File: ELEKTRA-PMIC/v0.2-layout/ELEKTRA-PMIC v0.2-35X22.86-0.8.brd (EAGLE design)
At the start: 35 x 22.9 mm, 96 parts, among them U1 BQ24195L, U4 MAX1704X

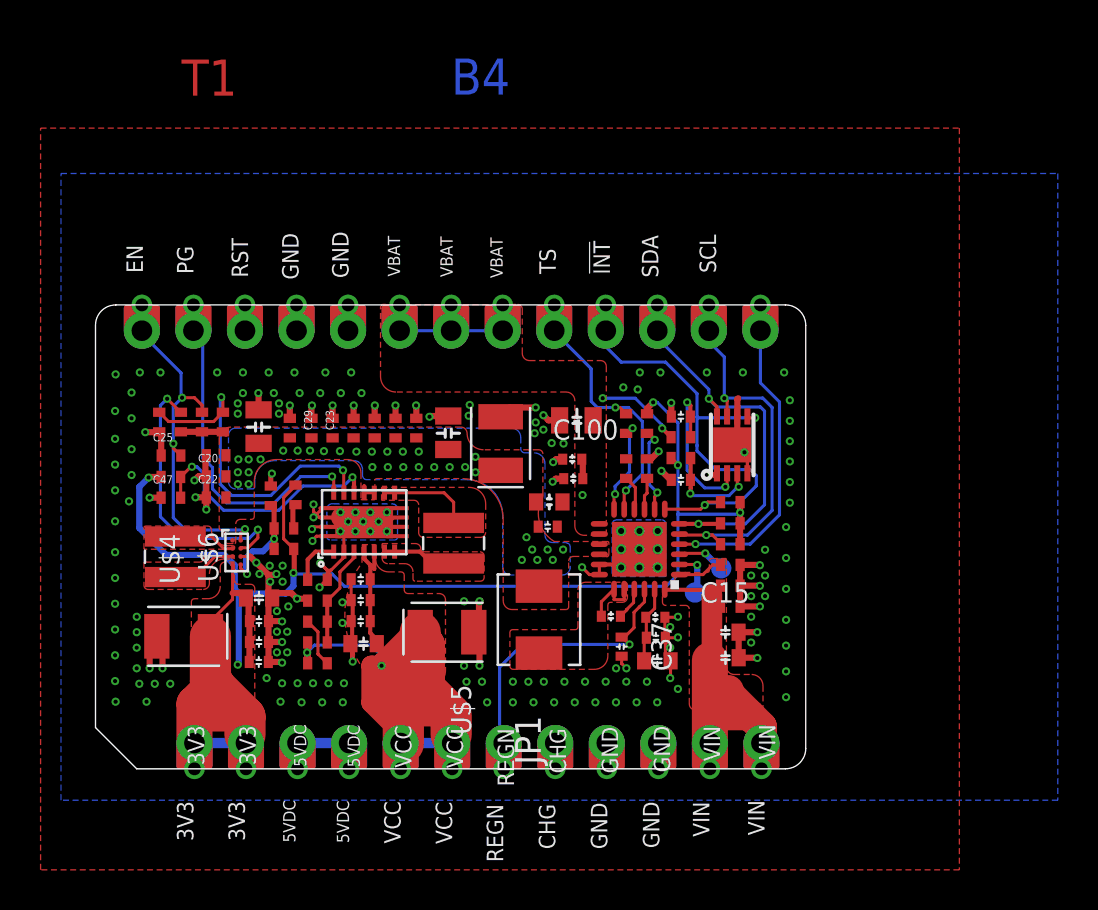
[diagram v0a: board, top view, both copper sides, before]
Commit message: update layout
complete the layout for power module
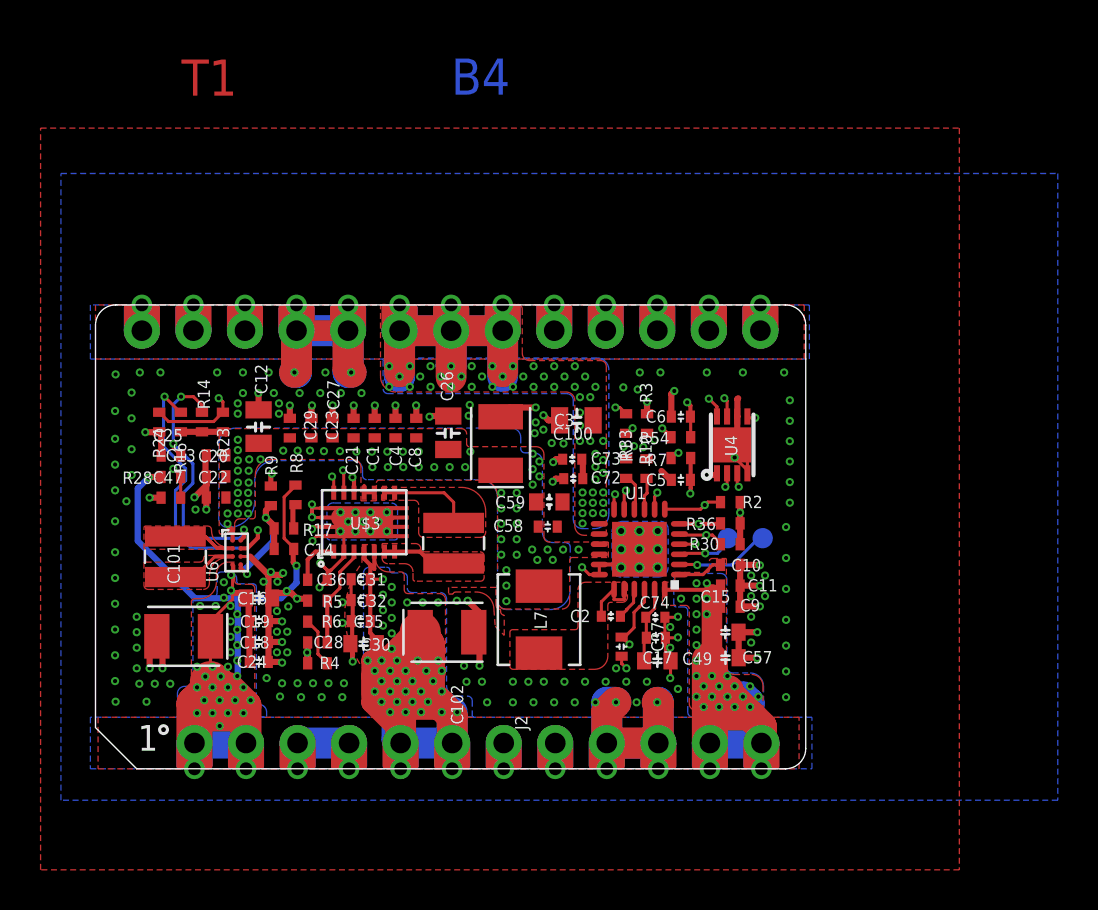
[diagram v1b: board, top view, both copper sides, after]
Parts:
- removed TP20, TP21, TP22: TP0.4MM, particle SZ:TP0.4MM
- C101: value CAP-ECASE_B -> 220uF.6V
- C102: value CAP-ECASE_B -> 220uF,6V
- TP10, TP11, TP3, TP4, TP5, TP6, TP7, TP8, TP9: value TP -> TP0.4MM; device particle SZ:TP0.7MM -> particle SZ:TP0.4MM
- moved TP1 4.28 mm to (32.9, 11.4)
- moved TP2 1.52 mm to (31.2, 11.4)
- moved TP17 0.60 mm to (12.8, 11.7)
- renumbered JP1 to J2, U$1 to J1, U$4 to C101, U$5 to C102, U$6 to U6
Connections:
- removed net PMID: J2.8, J2.@8
- net GND: no longer TP20.P$1, TP21.P$1, TP22.P$1
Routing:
- net GND: track 97.9 -> 135.2 mm, vias 188 -> 186
- net VBAT: track 14.8 -> 39.2 mm, vias 3 -> 54
- net 3V3: track 88.5 -> 107.4 mm, vias 6 -> 38
- net VIN: track 24.7 -> 32.9 mm, vias 0 -> 26
- net PG: track 17.9 -> 25.4 mm
- net N$22: track 16.8 -> 23.2 mm
- net VCC: track 47.4 -> 52.9 mm, vias 2 -> 41
- net N$21: track 12.8 -> 17.8 mm
- net TS: track 13.9 -> 17.8 mm
- net SCL: track 21.8 -> 24.4 mm
- net !FUEL-INT: track 23.4 -> 20.8 mm
- net N$7: track 2.81 -> 4.66 mm
- net N$12: track 3.07 -> 4.66 mm
- net VSYS: track 7.07 -> 8.66 mm, vias 33 -> 59
- net PMID: track 1.45 -> 0.00 mm
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- added copper zone on layer 15, net 3V3
- added copper zone on layer 16, net 3V3
- added copper zone on layer 2, net 3V3
- added copper zone on layer 15, net VBAT
- added copper zone on layer 16, net VBAT
- added copper zone on layer 2, net VBAT
- added copper zone on layer 15, net VCC
- added copper zone on layer 16, net VCC
- added copper zone on layer 2, net VCC
- added copper zone on layer 15, net VIN
- added copper zone on layer 16, net VIN
- added copper zone on layer 2, net VIN
- added copper zone on layer 2, net VSYS
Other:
- board text added: "1"
- board text added: "20240309"
- board text added: "NC"
- board text removed: "20240223"

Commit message: update layout
Optimize routing
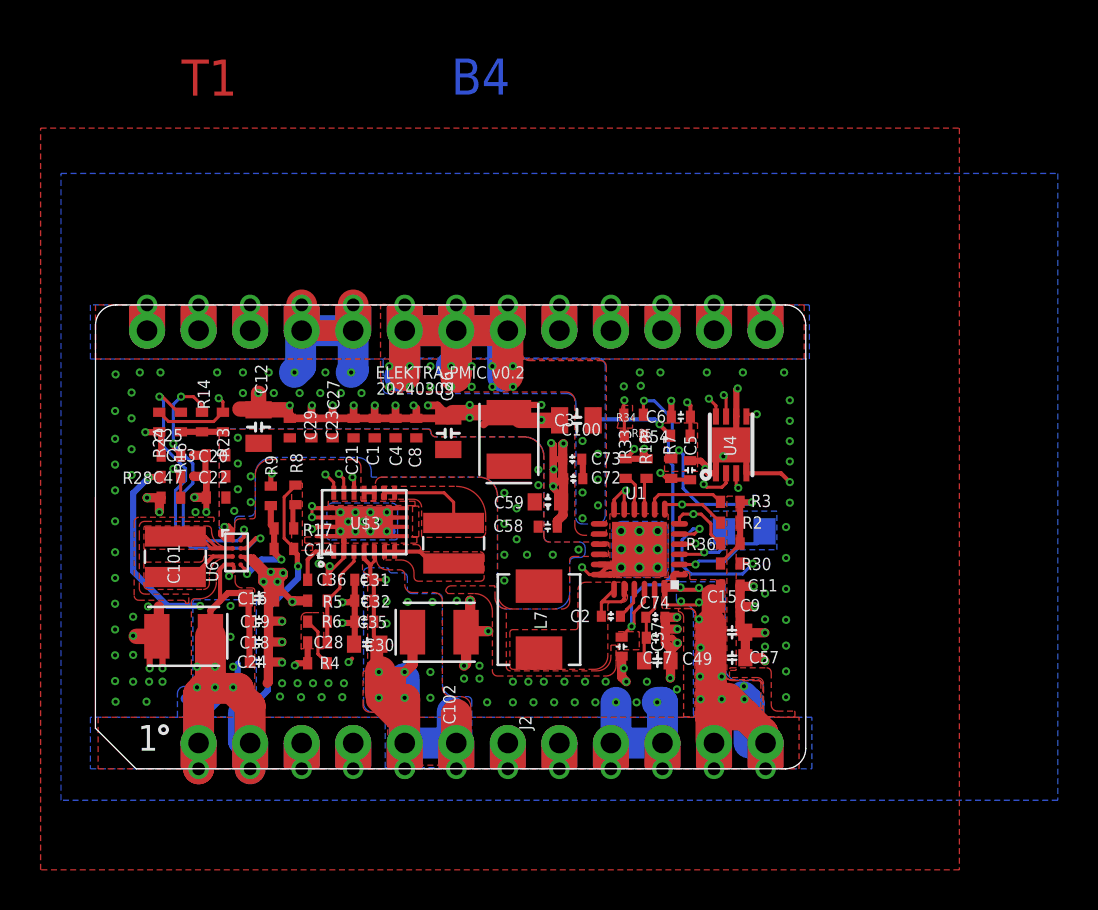
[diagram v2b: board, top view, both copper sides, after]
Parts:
- removed C10: 100pF, Particle:C0402_B
- removed R1: 0R, Spark:R0402_B
- added R34: 31.2K, Spark:R0402_B
- added R35: 5.49K, Spark:R0402_B
- R14: value 1M -> 100K
- TP1, TP2: value TPTP -> TP1311MM; device particle SZ:TP -> particle SZ:TP-1311MM
- moved R3 5.63 mm to (31.3, 13.2), turned to 180 degrees
- moved R2 1.02 mm to (31.3, 12.1)
- moved R36 0.99 mm to (31.3, 11.1)
- moved R30 0.95 mm to (31.3, 10.1), turned to 0 degrees
- moved R7 0.71 mm to (28.4, 14.8), turned to 270 degrees
- moved C5 0.66 mm to (29.3, 14.7), turned to 90 degrees
- moved C100 0.45 mm to (20.4, 16.2)
- moved TP2 0.38 mm to (31.0, 11.7), turned to 180 degrees
- moved C102 0.38 mm to (16.9, 6.73)
- moved TP1 0.34 mm to (33.0, 11.7), turned to 180 degrees
- moved C15 0.33 mm to (31.4, 6.73)
- moved C57 0.33 mm to (31.4, 5.47)
- moved J1 0.25 mm to (17.8, 21.6)
- moved J2 0.20 mm to (19.1, 1.27)
- moved C32 0.18 mm to (13.2, 8.29)
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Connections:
- removed net N$1: R1.1, U1.12
- net GND: now also R34.2; no longer C10.1
- net REGN: now also R35.1
- net TS: now also R34.1, R35.2, U1.12; no longer R1.2
- net VIN: no longer C10.2
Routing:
- net GND: track 135.2 -> 211.1 mm, vias 186 -> 165
- net REGN: track 15.2 -> 32.1 mm, vias 1 -> 2
- net VIN: track 32.9 -> 46.9 mm, vias 26 -> 12
- net VCC: track 52.9 -> 61.1 mm, vias 41 -> 12
- net 3V3: track 107.4 -> 115.4 mm, vias 38 -> 14
- net SCL: track 24.4 -> 31.5 mm, vias 2 -> 3
- net N$1: track 5.25 -> 0.00 mm, vias 2 -> 0
- net VSYS: track 8.66 -> 13.8 mm, vias 59 -> 18
- net 5VDC: track 5.08 -> 10.2 mm
- net !FUEL-INT: track 20.8 -> 25.0 mm
- net VBAT: track 39.2 -> 43.0 mm, vias 54 -> 21
- net SDA: track 22.0 -> 25.2 mm
- net !RST: track 1.95 -> 4.54 mm
- net ENABLE: track 19.6 -> 22.1 mm
- net N$48: track 5.50 -> 7.84 mm
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- added copper zone on layer 1, net N$3
- removed copper zone on layer 2, net 3V3
- removed copper zone on layer 2, net VBAT
- removed copper zone on layer 2, net VCC
- removed copper zone on layer 2, net VIN
- removed copper zone on layer 2, net VSYS
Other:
- outline, holes or cut-outs redrawn
